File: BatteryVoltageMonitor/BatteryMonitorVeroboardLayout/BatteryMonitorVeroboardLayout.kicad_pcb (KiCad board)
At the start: 2 copper layers, 100 x 50 mm, 23 parts, among them J1 Screw_Terminal_01x03, J2 Conn_01x03, Q1 IRLB8721PBF, U1 SX1278 LoRa Module, U2 MIC2954, U3 PICAXE-14M, U4 DS18B20

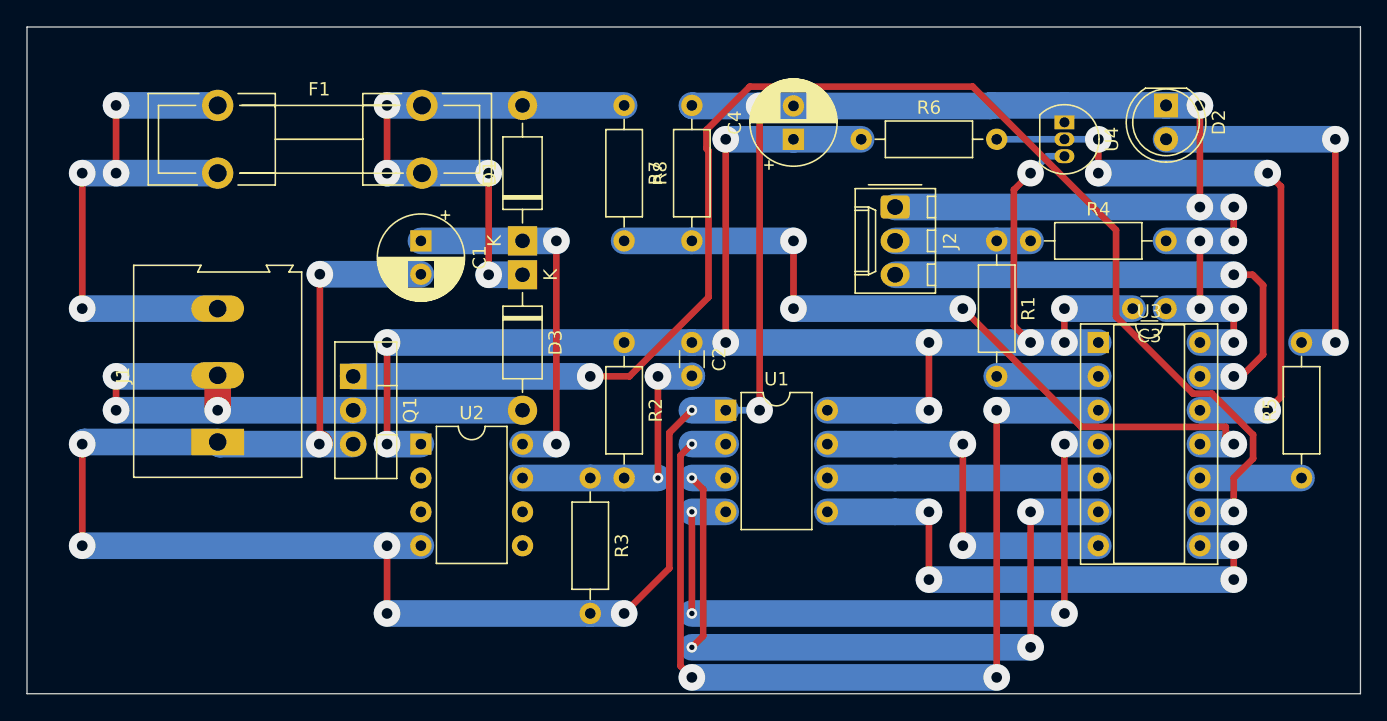
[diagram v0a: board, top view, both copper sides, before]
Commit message: Updated battery and pump monitor KiCAD files to be openable
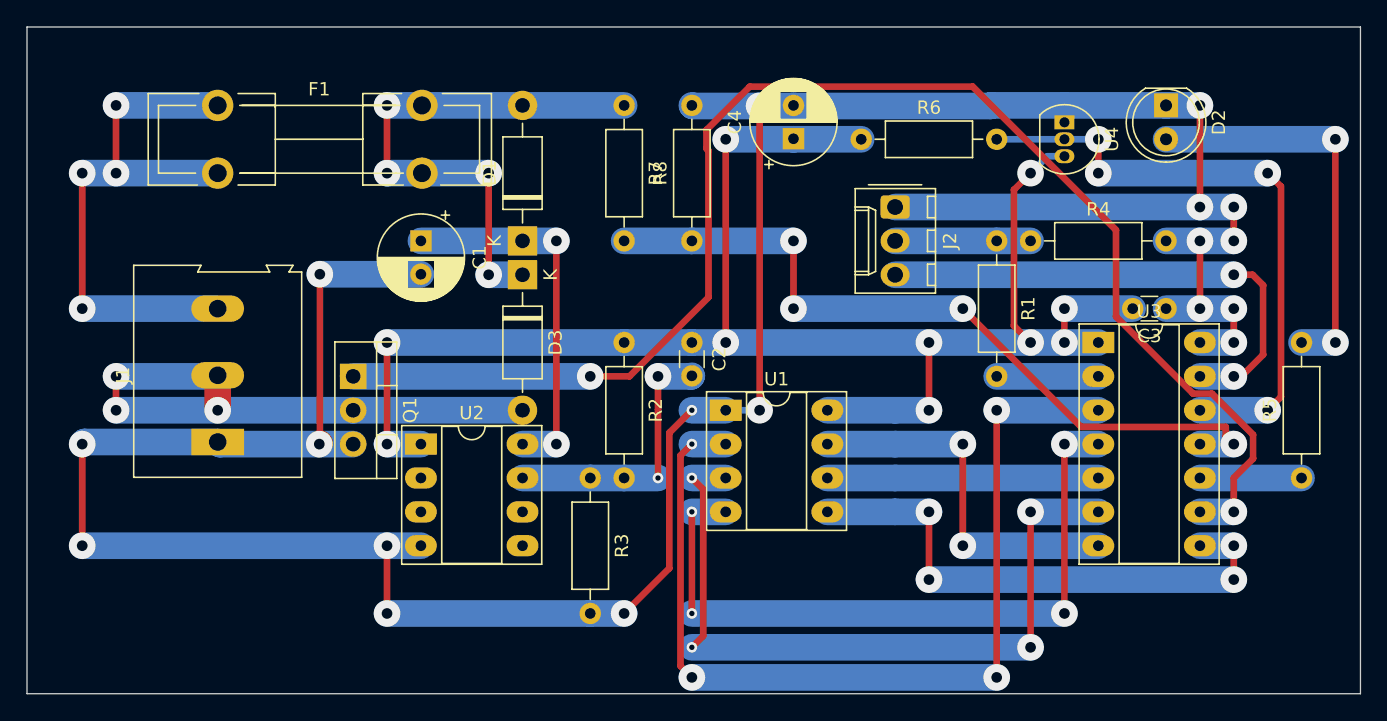
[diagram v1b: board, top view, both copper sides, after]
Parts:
- C1: value 100uF -> 100u
- C4: value 3.3uF -> 3.3u
- F1: footprint Fuse Holders Custom:Fuseholder5x20_horiz_open_lateral_Type-II -> Custom:Fuseholder5x20_horiz_open_lateral_Type-II
- U1: value SX1278 LoRa Module -> Ra01_Breakout_Module; footprint Package_DIP:DIP-8_W7.62mm -> Package_DIP:DIP-8_W7.62mm_Socket_LongPads
- U2: footprint Package_DIP:DIP-8_W7.62mm -> Package_DIP:DIP-8_W7.62mm_Socket_LongPads
- U3: value PICAXE-14M -> PICAXE-14M2; footprint Package_DIP:DIP-14_W7.62mm_Socket -> Package_DIP:DIP-14_W7.62mm_Socket_LongPads
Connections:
- net +3V3 renamed +3.3V
- D3 pad 1: +BATT -> Net-(D3-K)
- F1 pad 1: Net-(F1-Pad1) -> Net-(D3-K)
- J1 pad 3: Net-(F1-Pad1) -> Net-(D3-K)
- U2 pad 2: Net-(U2-Pad2) -> unconnected-(U2-SNS-Pad2)
- U2 pad 3: Net-(U2-Pad3) -> unconnected-(U2-SHDN-Pad3)
- U2 pad 5: Net-(U2-Pad5) -> unconnected-(U2-/ERR-Pad5)
- U2 pad 6: Net-(U2-Pad6) -> unconnected-(U2-TAP-Pad6)
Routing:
- net Net-(F1-Pad1): track 43.2 -> 0.00 mm, vias 4 -> 0
- net Net-(D3-K): track 0.00 -> 43.2 mm, vias 0 -> 4
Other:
- net class Default removed
